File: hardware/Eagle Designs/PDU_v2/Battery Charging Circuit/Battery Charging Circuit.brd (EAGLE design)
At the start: 50 x 50 mm, 29 parts, among them J1 5037630291, J2 5037630291, U1 LTC4012IUFPBF, U2 SI4431BDY-T1-E3, U3 AO4818B

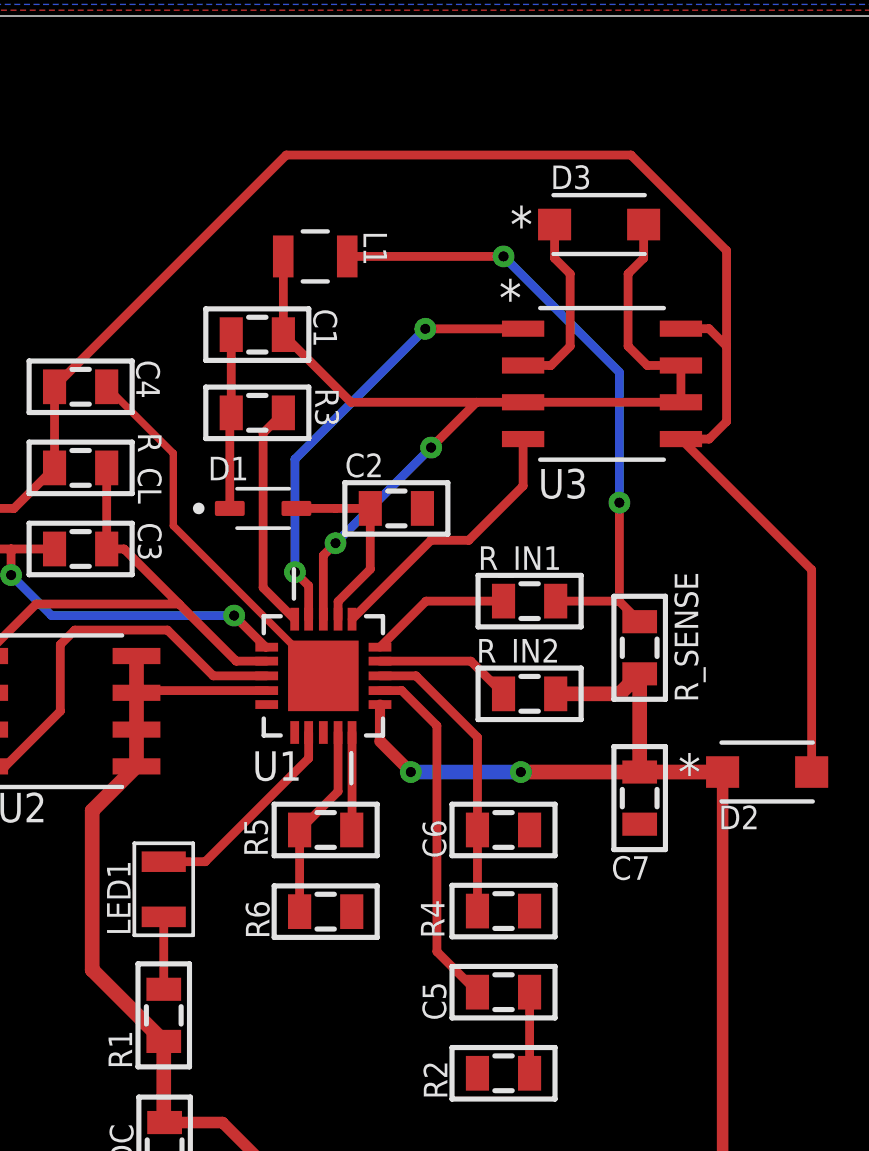
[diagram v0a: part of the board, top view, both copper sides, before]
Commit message: Finalized PDU Battery Charging Circuit Design And Added Gerber Files
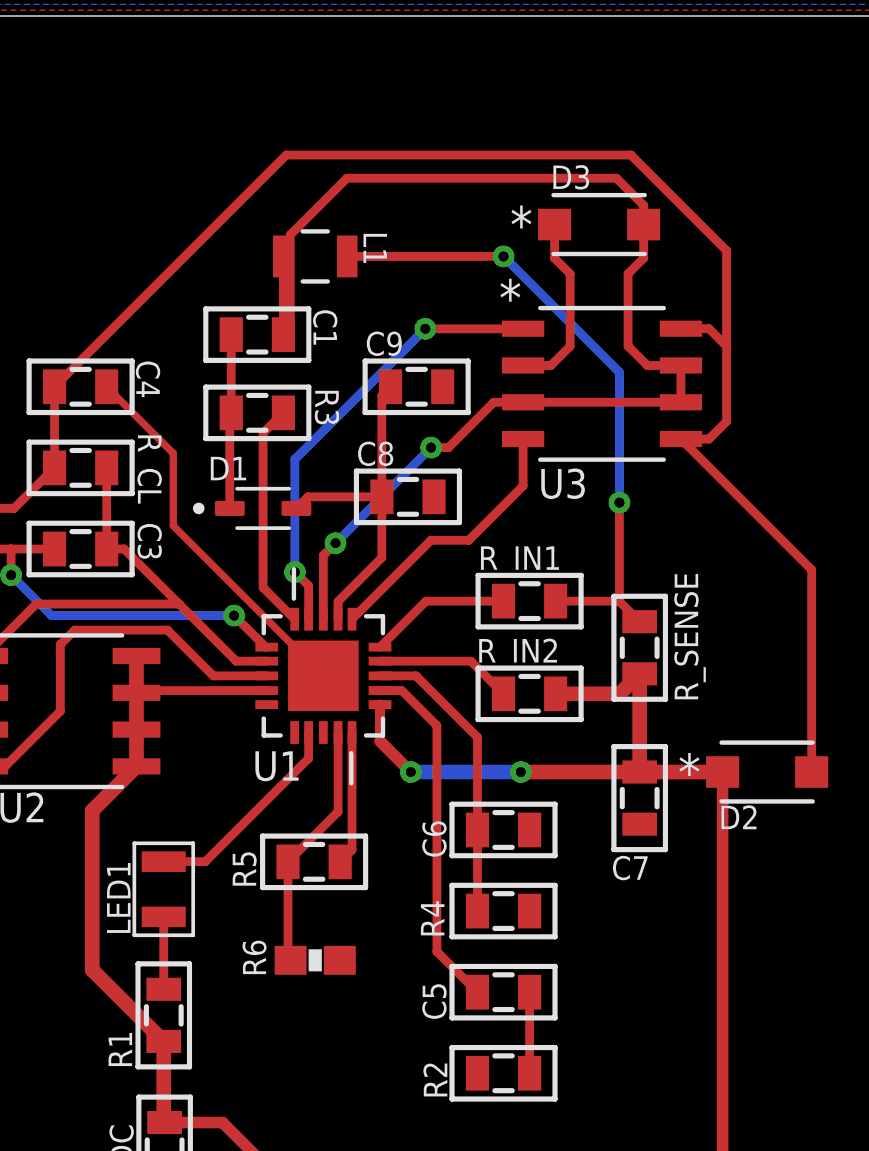
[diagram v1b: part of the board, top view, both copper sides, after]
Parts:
- removed C2: 2 uF, HSFL_Main_Library:0805
- added C8, C9: 1 uF, HSFL_Main_Library:0805
- R6: value 28.4 k -> 28.4k; device HSFL_Main_Library:0805 -> HSFL_Main_Library:0603-RES
- moved R6 1.72 mm to (19.6, 17.4), turned to 180 degrees
- moved R5 1.17 mm to (19.6, 20.8)
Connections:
- net GND: now also C8.2, C9.2, R6.1; no longer C2.2, R6.2
- net N$16: now also R6.2; no longer R6.1
- net N$9: now also C8.1, C9.1; no longer C2.1
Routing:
- net SW: track 34.9 -> 44.8 mm
- net N$9: track 6.83 -> 11.9 mm
- net N$16: track 6.73 -> 8.62 mm
- net N$15: track 3.37 -> 4.63 mm
